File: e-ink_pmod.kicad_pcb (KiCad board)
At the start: 2 copper layers, 45.7 x 20.3 mm, 23 parts, among them Q1 Q_NMOS_GSD, U1 23K640-I/SN, X1 52435-2471

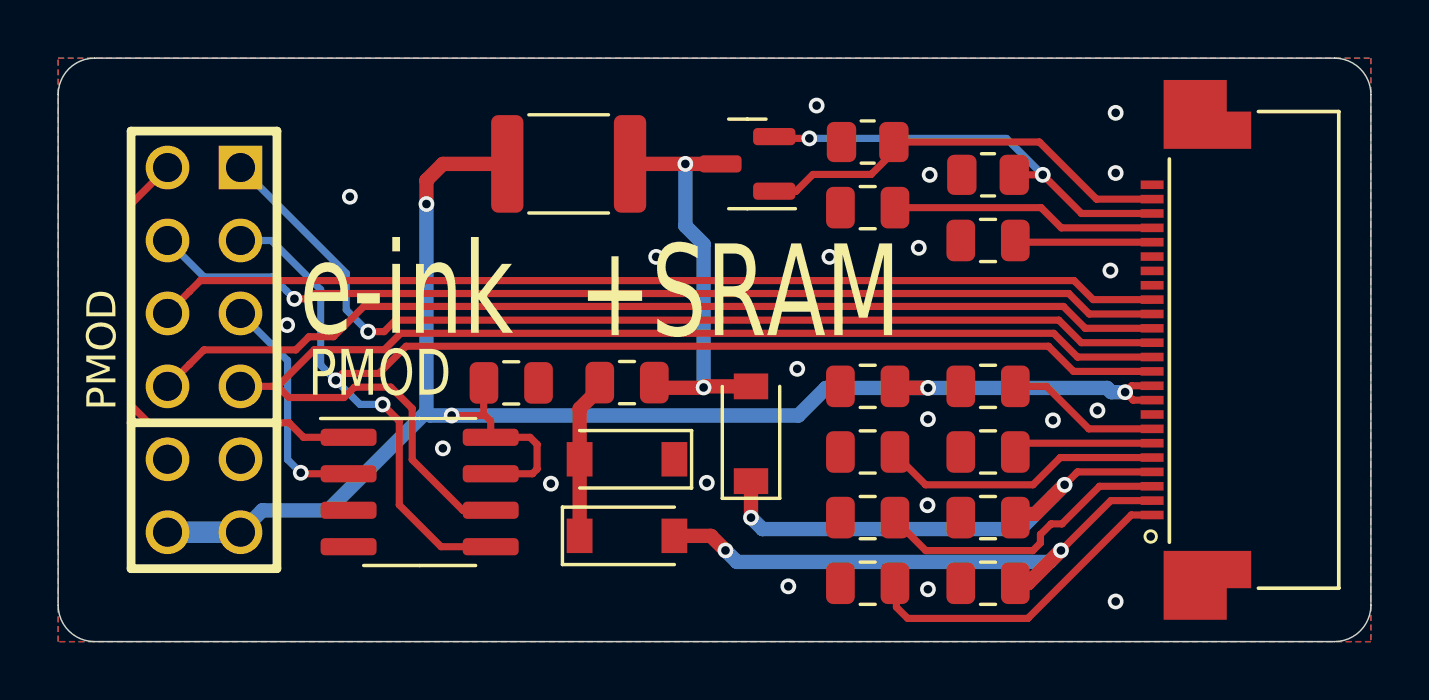
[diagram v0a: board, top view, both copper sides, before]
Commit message: Updated documentation
Also updated KiCad version for better compatibility with KiCanvas

Signed-off-by: Thomas Flummer <tf@flummer.net>
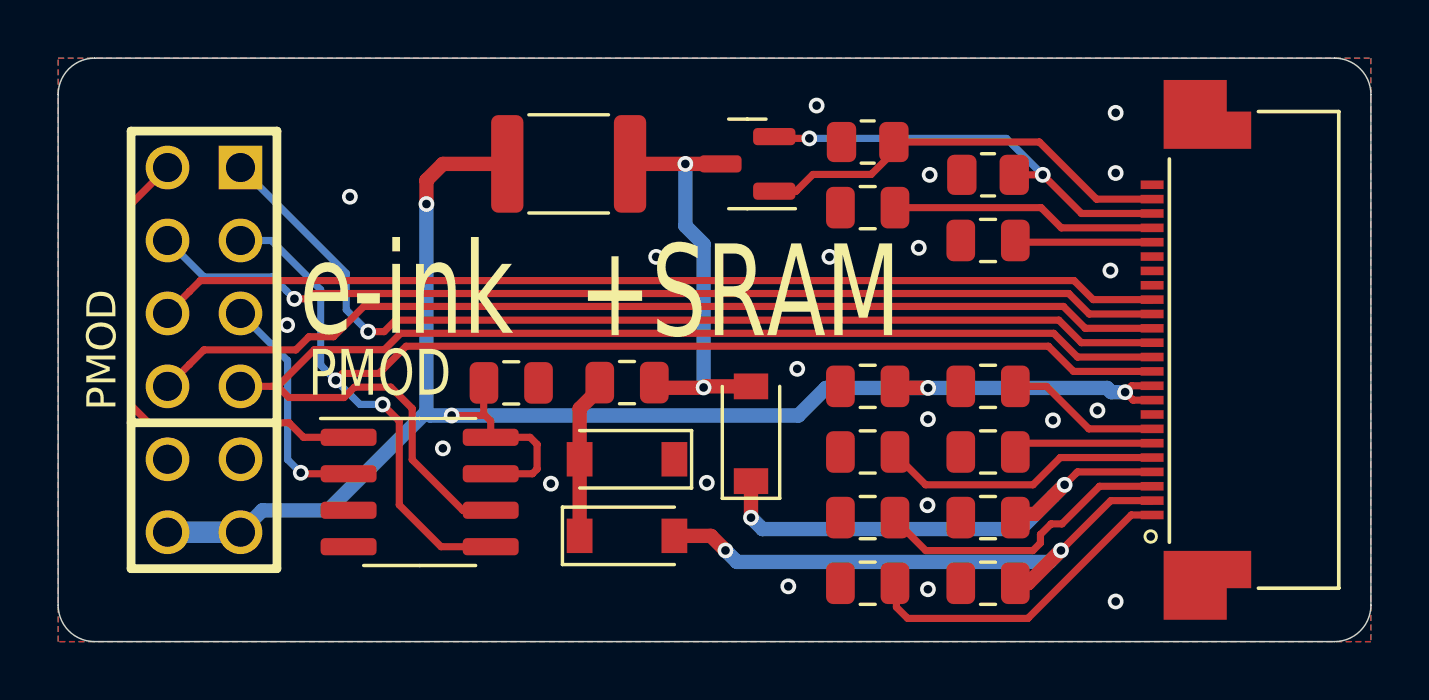
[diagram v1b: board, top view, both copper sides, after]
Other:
- board text added: "~{BUSY}"
- board text added: "~{D/C}"
- board text added: "~{EINKCS}"
- board text added: "~{RESET}"
- board text added: "~{SRAMCS}"
- board text removed: "~BUSY"
- board text removed: "~D/C"
- board text removed: "~EINKCS"
- board text removed: "~RESET"
- board text removed: "~SRAMCS"
